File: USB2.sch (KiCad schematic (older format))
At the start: 0 parts

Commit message: Added relevant main components to the sheet USB2.sch sheet
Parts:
- added C?: C_Small, Capacitor_SMD:C_0603_1608Metric_Pad1.08x0.95mm_HandSolder, symbol Device:C_Small
- added C?: C_Polarized_Small, Capacitor_Tantalum_SMD:CP_EIA-1608-10_AVX-L_Pad1.25x1.05mm_HandSolder, symbol Device:C_Polarized_Small
- added C?: C_Small, symbol Device:C_Small
- added IC?: USB3320C-EZK, GM_QFN:QFN50P500X500X100-33N-D, symbol GM_Interface_IC:USB3320C-EZK
- added J?: 0475890001, digikey-footprints:USB_Micro_AB_Female_0475890001, symbol dk_USB-DVI-HDMI-Connectors:0475890001
- added J?: UE27AC54100, digikey-footprints:USB_A_Female_UE27AC54100, symbol dk_USB-DVI-HDMI-Connectors:UE27AC54100
- added R?: R_Small_US, Resistor_SMD:R_0603_1608Metric_Pad0.98x0.95mm_HandSolder, symbol Device:R_Small_US
- added U?: TPS2051BDBVR, digikey-footprints:SOT-753, symbol dk_PMIC-Power-Distribution-Switches-Load-Drivers:TPS2051BDBVR
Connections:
- net labels added: GNDD, VCC3V3
- wire segments 0 -> 2
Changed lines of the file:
@@
 Comment4 ""
 $EndDescr
+$Comp
+L GM_Interface_IC:USB3320C-EZK IC?
+U 1 1 602DDF35
+P 2850 2400
+F 0 "IC?" H 3300 2565 50  0000 C CNN
+F 1 "USB3320C-EZK" H 3300 2474 50  0000 C CNN
+F 2 "GM_QFN:QFN50P500X500X100-33N-D" H 4400 2100 50  0001 L CNN
+F 3 "https://ww1.microchip.com/downloads/en/DeviceDoc/00001792E.pdf" H 4400 2000 50  0001 L CNN
+F 4 "USB3320C-EZK" H 4750 2200 50  0001 C CNN "MPN"
+	1    2850 2400
+	1    0    0    -1
+$EndComp
+$Comp
+L dk_PMIC-Power-Distribution-Switches-Load-Drivers:TPS2051BDBVR U?
+U 1 1 602E0070
+P 6200 4000
+F 0 "U?" H 6200 4287 60  0000 C CNN
+F 1 "TPS2051BDBVR" H 6200 4181 60  0000 C CNN
+F 2 "digikey-footprints:SOT-753" H 6400 4200 60  0001 L CNN
+F 3 "http://www.ti.com/general/docs/suppproductinfo.tsp?distId=10&gotoUrl=http%3A%2F%2Fwww.ti.com%2Flit%2Fgpn%2Ftps2051b" H 6400 4300 60  0001 L CNN
+F 4 "296-21265-1-ND" H 6400 4400 60  0001 L CNN "Digi-Key_PN"
+F 5 "TPS2051BDBVR" H 6400 4500 60  0001 L CNN "MPN"
+F 6 "Integrated Circuits (ICs)" H 6400 4600 60  0001 L CNN "Category"
+F 7 "PMIC - Power Distribution Switches, Load Drivers" H 6400 4700 60  0001 L CNN "Family"
+F 8 "http://www.ti.com/general/docs/suppproductinfo.tsp?distId=10&gotoUrl=http%3A%2F%2Fwww.ti.com%2Flit%2Fgpn%2Ftps2051b" H 6400 4800 60  0001 L CNN "DK_Datasheet_Link"
+F 9 "/product-detail/en/texas-instruments/TPS2051BDBVR/296-21265-1-ND/1219985" H 6400 4900 60  0001 L CNN "DK_Detail_Page"
+F 10 "IC PWR DIST SWITCH SNGL SOT23-5" H 6400 5000 60  0001 L CNN "Description"
+F 11 "Texas Instruments" H 6400 5100 60  0001 L CNN "Manufacturer"
+F 12 "Active" H 6400 5200 60  0001 L CNN "Status"
+	1    6200 4000
+	1    0    0    -1
+$EndComp
+$Comp
+L dk_USB-DVI-HDMI-Connectors:0475890001 J?
+U 1 1 602E0AAF
+P 8600 2550
+F 0 "J?" H 8663 3275 50  0000 C CNN
+F 1 "0475890001" H 8663 3184 50  0000 C CNN
+F 2 "digikey-footprints:USB_Micro_AB_Female_0475890001" H 8800 2750 60  0001 L CNN
+F 3 "https://www.molex.com/pdm_docs/sd/475890001_sd.pdf" H 8800 2850 60  0001 L CNN
+F 4 "WM17143CT-ND" H 8800 2950 60  0001 L CNN "Digi-Key_PN"
+F 5 "0475890001" H 8800 3050 60  0001 L CNN "MPN"
+F 6 "Connectors, Interconnects" H 8800 3150 60  0001 L CNN "Category"
+F 7 "USB, DVI, HDMI Connectors" H 8800 3250 60  0001 L CNN "Family"
+F 8 "https://www.molex.com/pdm_docs/sd/475890001_sd.pdf" H 8800 3350 60  0001 L CNN "DK_Datasheet_Link"
+F 9 "/product-detail/en/molex/0475890001/WM17143CT-ND/1832255" H 8800 3450 60  0001 L CNN "DK_Detail_Page"
+F 10 "CONN RCPT MICRO USB AB 5P SMD RA" H 8800 3550 60  0001 L CNN "Description"
+F 11 "Molex" H 8800 3650 60  0001 L CNN "Manufacturer"
+F 12 "Active" H 8800 3750 60  0001 L CNN "Status"
+	1    8600 2550
+	-1   0    0    -1
+$EndComp
+$Comp
+L dk_USB-DVI-HDMI-Connectors:UE27AC54100 J?
+U 1 1 602E160D
+P 8650 4750
+F 0 "J?" H 8770 5262 60  0000 C CNN
+F 1 "UE27AC54100" H 8770 5156 60  0000 C CNN
+F 2 "digikey-footprints:USB_A_Female_UE27AC54100" H 8850 4950 60  0001 L CNN
+F 3 "https://www.amphenolcanada.com/ProductSearch/drawings/AC/UE27ACX4X0X.pdf" H 8850 5050 60  0001 L CNN
+F 4 "UE27AC54100-ND" H 8850 5150 60  0001 L CNN "Digi-Key_PN"
+F 5 "UE27AC54100" H 8850 5250 60  0001 L CNN "MPN"
+F 6 "Connectors, Interconnects" H 8850 5350 60  0001 L CNN "Category"
+F 7 "USB, DVI, HDMI Connectors" H 8850 5450 60  0001 L CNN "Family"
+F 8 "https://www.amphenolcanada.com/ProductSearch/drawings/AC/UE27ACX4X0X.pdf" H 8850 5550 60  0001 L CNN "DK_Datasheet_Link"
+F 9 "/product-detail/en/amphenol-icc-commercial-products/UE27AC54100/UE27AC54100-ND/1972253" H 8850 5650 60  0001 L CNN "DK_Detail_Page"
+F 10 "CONN RCPT USB2.0 TYPEA 4POS R/A" H 8850 5750 60  0001 L CNN "Description"
+F 11 "Amphenol ICC (Commercial Products)" H 8850 5850 60  0001 L CNN "Manufacturer"
+F 12 "Active" H 8850 5950 60  0001 L CNN "Status"
+	1    8650 4750
+	-1   0    0    -1
+$EndComp
+$Comp
+L Device:R_Small_US R?
+U 1 1 602EE6FB
+P -1100 700
+AR Path="/601E7C5A/602EE6FB" Ref="R?"  Part="1"
+AR Path="/601E7CC8/602EE6FB" Ref="R?"  Part="1"
+AR Path="/601E7C92/602EE6FB" Ref="R?"  Part="1"
+AR Path="/601E7C92/60257FE5/602EE6FB" Ref="R?"  Part="1"
+AR Path="/601E7B38/602EE6FB" Ref="R?"  Part="1"
+F 0 "R?" H -1032 746 50  0000 L CNN
+F 1 "R_Small_US" H -1032 655 50  0000 L CNN
+F 2 "Resistor_SMD:R_0603_1608Metric_Pad0.98x0.95mm_HandSolder" H -1100 700 50  0001 C CNN
+F 3 "~" H -1100 700 50  0001 C CNN
+	1    -1100 700
+	1    0    0    -1
+$EndComp
+$Comp
+L Device:C_Small C?
+U 1 1 602EE702
+P -1800 700
+AR Path="/601E7C5A/602EE702" Ref="C?"  Part="1"
+AR Path="/601E7CC8/602EE702" Ref="C?"  Part="1"
+AR Path="/601E7C92/602EE702" Ref="C?"  Part="1"
+AR Path="/601E7C92/60257FE5/602EE702" Ref="C?"  Part="1"
+AR Path="/601E7B38/602EE702" Ref="C?"  Part="1"
+F 0 "C?" H -1708 746 50  0000 L CNN
+F 1 "C_Small" H -1708 655 50  0000 L CNN
+F 2 "Capacitor_SMD:C_0603_1608Metric_Pad1.08x0.95mm_HandSolder" H -1800 700 50  0001 C CNN
+F 3 "~" H -1800 700 50  0001 C CNN
+F 4 "" H -1800 700 50  0000 C CNN "Voltage"
+	1    -1800 700
+	1    0    0    -1
+$EndComp
+Text GLabel -1600 1300 0    50   Input ~ 0
+VCC3V3
+$Comp
+L power:PWR_FLAG #FLG?
+U 1 1 602EE709
+P -1400 1300
+AR Path="/601E7C5A/602EE709" Ref="#FLG?"  Part="1"
+AR Path="/601E7CC8/602EE709" Ref="#FLG?"  Part="1"
+AR Path="/601E7C92/602EE709" Ref="#FLG?"  Part="1"
+AR Path="/601E7C92/60257FE5/602EE709" Ref="#FLG?"  Part="1"
+AR Path="/601E7B38/602EE709" Ref="#FLG?"  Part="1"
+F 0 "#FLG?" H -1400 1375 50  0001 C CNN
+F 1 "PWR_FLAG" H -1400 1473 50  0000 C CNN
+F 2 "" H -1400 1300 50  0001 C CNN
+F 3 "~" H -1400 1300 50  0001 C CNN
+	1    -1400 1300
+	1    0    0    -1
+$EndComp
+Connection ~ -1400 1300
+Wire Wire Line
+	-1400 1300 -1200 1300
+Wire Wire Line
+	-1600 1300 -1400 1300
+$Comp
+L power:GNDD #PWR?
+U 1 1 602EE712
+P -900 950
+AR Path="/601DF0A6/602EE712" Ref="#PWR?"  Part="1"
+AR Path="/601E7C5A/602EE712" Ref="#PWR?"  Part="1"
+AR Path="/601E7CC8/602EE712" Ref="#PWR?"  Part="1"
+AR Path="/601E7C92/602EE712" Ref="#PWR?"  Part="1"
+AR Path="/601E7C92/60257FE5/602EE712" Ref="#PWR?"  Part="1"
+AR Path="/601E7B38/602EE712" Ref="#PWR?"  Part="1"
+F 0 "#PWR?" H -900 700 50  0001 C CNN
+F 1 "GNDD" H -896 795 50  0000 C CNN
+F 2 "" H -900 950 50  0001 C CNN
+F 3 "" H -900 950 50  0001 C CNN
+	1    -900 950
+	1    0    0    -1
+$EndComp
+$Comp
+L Device:C_Polarized_Small C?
+U 1 1 602EE719
+P -1500 450
+AR Path="/601E7C92/602EE719" Ref="C?"  Part="1"
+AR Path="/601E7C92/60257FE5/602EE719" Ref="C?"  Part="1"
+AR Path="/601E7B38/602EE719" Ref="C?"  Part="1"
+F 0 "C?" H -1412 496 50  0000 L CNN
+F 1 "C_Polarized_Small" H -1412 405 50  0000 L CNN
+F 2 "Capacitor_Tantalum_SMD:CP_EIA-1608-10_AVX-L_Pad1.25x1.05mm_HandSolder" H -1500 450 50  0001 C CNN
+F 3 "~" H -1500 450 50  0001 C CNN
+F 4 "" H -1500 450 50  0000 C CNN "Voltage"
+	1    -1500 450
+	1    0    0    -1
+$EndComp
+$Comp
+L Device:C_Small C?
+U 1 1 602EE71F
+P -300 500
+F 0 "C?" V -529 500 50  0000 C CNN
+F 1 "C_Small" V -438 500 50  0000 C CNN
+F 2 "" H -300 500 50  0001 C CNN
+F 3 "~" H -300 500 50  0001 C CNN
+	1    -300 500
+	0    1    1    0
+$EndComp
 $EndSCHEMATC

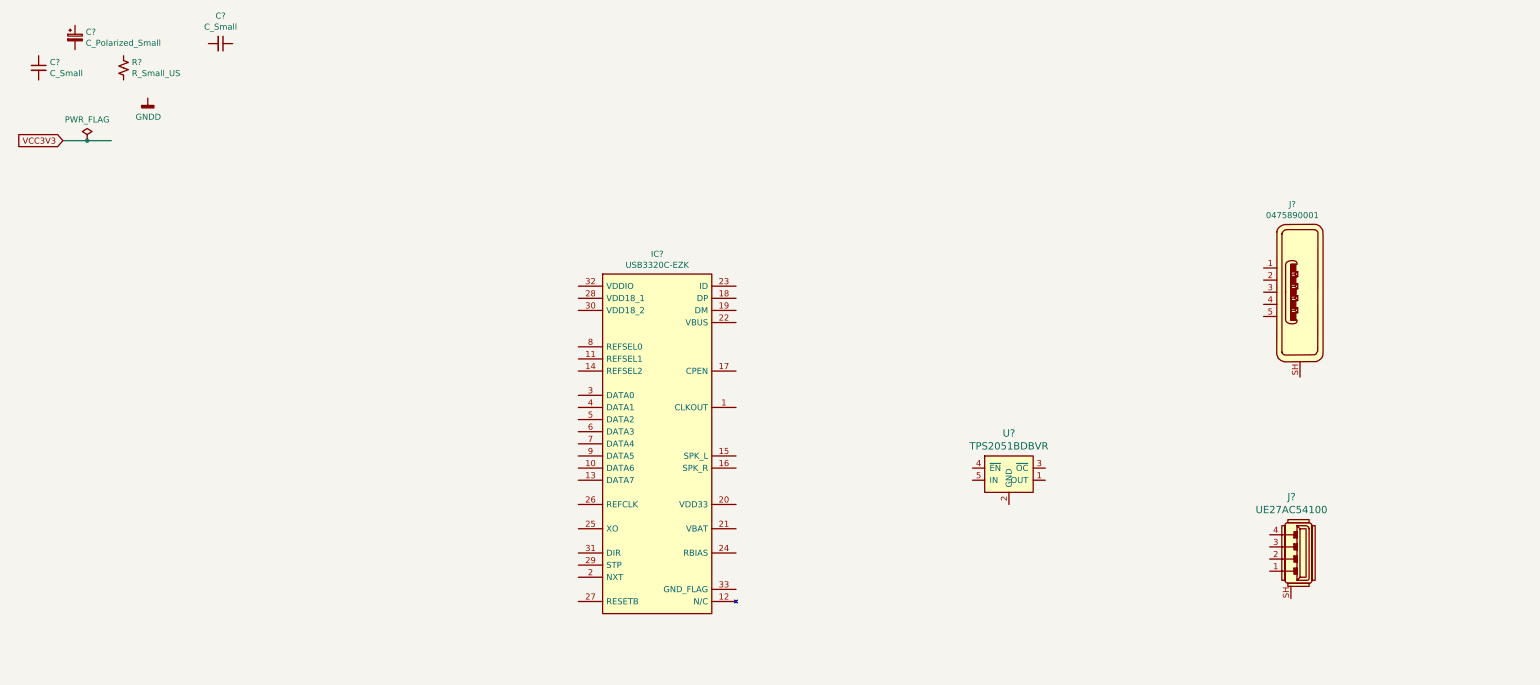
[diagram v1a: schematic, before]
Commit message: Drawn USB2 schematics
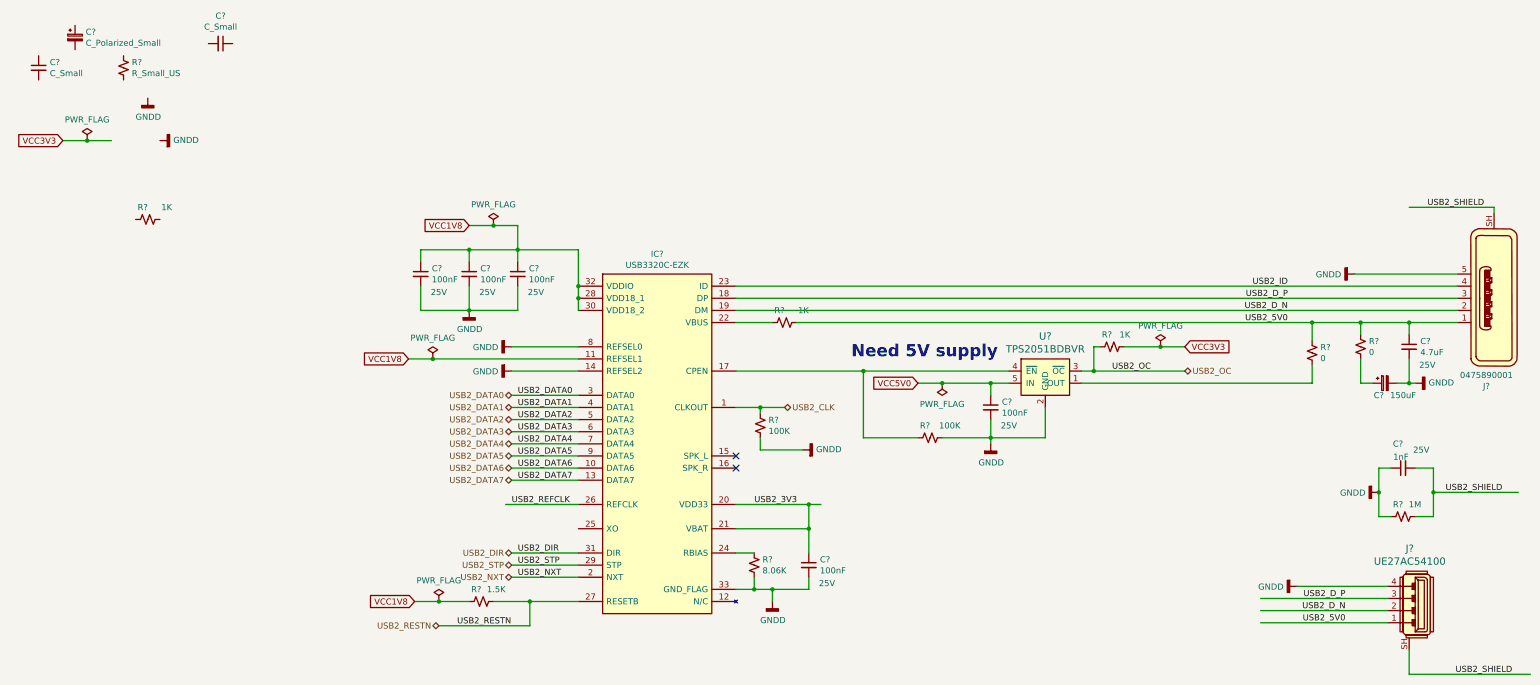
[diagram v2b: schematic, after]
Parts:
- added C? (x5): 100nF, Capacitor_SMD:C_0603_1608Metric_Pad1.08x0.95mm_HandSolder, symbol Device:C_Small
- added C?: 1nF, Capacitor_SMD:C_0603_1608Metric_Pad1.08x0.95mm_HandSolder, symbol Device:C_Small
- added C?: 4.7uF, Capacitor_SMD:C_0603_1608Metric_Pad1.08x0.95mm_HandSolder, symbol Device:C_Small
- added C?: 150uF, symbol Device:C_Polarized_Small
- added R?: 1.5K, Resistor_SMD:R_0603_1608Metric_Pad0.98x0.95mm_HandSolder, symbol Device:R_Small_US
- added R? (x3): 1K, Resistor_SMD:R_0603_1608Metric_Pad0.98x0.95mm_HandSolder, symbol Device:R_Small_US
- added R? (x2): 100K, Resistor_SMD:R_0603_1608Metric_Pad0.98x0.95mm_HandSolder, symbol Device:R_Small_US
- added R?: 8.06K, Resistor_SMD:R_0603_1608Metric_Pad0.98x0.95mm_HandSolder, symbol Device:R_Small_US
- added R?: 1M, Resistor_SMD:R_0603_1608Metric_Pad0.98x0.95mm_HandSolder, symbol Device:R_Small_US
- added R? (x2): 0, Resistor_SMD:R_0603_1608Metric_Pad0.98x0.95mm_HandSolder, symbol Device:R_Small_US
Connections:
- net labels added: USB2_3V3, USB2_5V0, USB2_CLK, USB2_DATA0, USB2_DATA1, USB2_DATA2, USB2_DATA3, USB2_DATA4, USB2_DATA5, USB2_DATA6, USB2_DATA7, USB2_DIR, USB2_D_N, USB2_D_P, USB2_ID, USB2_NXT, USB2_OC, USB2_REFCLK, USB2_RESTN, USB2_SHIELD, USB2_STP, VCC1V8, VCC5V0
- wire segments 2 -> 113
- no-connect marks 0 -> 2
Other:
- note added: "Need 5V supply"
- moved on the sheet: J?, U?
